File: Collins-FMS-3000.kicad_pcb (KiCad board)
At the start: 2 copper layers, 145 x 160 mm, 188 parts, among them J1 USB_B_Mini, J2 AVR-ISP-6, J3 Conn_01x04, SW1 SW_Push_LED, SW10 SW_Push_LED, SW11 SW_Push_LED, SW12 SW_Push_LED, SW13 SW_Push_LED, SW14 SW_Push_LED, SW15 SW_Push_LED, SW16 SW_Push_LED, SW17 SW_Push_LED, SW18 SW_Push_LED, SW19 SW_Push_LED, SW2 SW_Push_LED, SW20 SW_Push_LED, SW21 SW_Push_LED, SW22 SW_Push_LED, SW23 SW_Push_LED, SW24 SW_Push_LED, SW25 SW_Push_LED, SW26 SW_Push_LED, SW27 SW_Push_LED, SW28 SW_Push_LED, SW29 SW_Push_LED, SW3 SW_Push_LED, SW30 SW_Push_LED, SW31 SW_Push_LED, SW32 SW_Push_LED, SW33 SW_Push_LED, SW34 SW_Push_LED, SW35 SW_Push_LED, SW36 SW_Push_LED, SW37 SW_Push_LED, SW38 SW_Push_LED, SW39 SW_Push_LED, SW4 SW_Push_LED, SW40 SW_Push_LED, SW41 SW_Push_LED, SW42 SW_Push_LED, SW43 SW_Push_LED, SW44 SW_Push_LED, SW45 SW_Push_LED, SW46 SW_Push_LED, SW47 SW_Push_LED, SW48 SW_Push_LED, SW49 SW_Push_LED, SW5 SW_Push_LED, SW50 SW_Push_LED, SW51 SW_Push_LED, SW52 SW_Push_LED, SW53 SW_Push_LED, SW54 SW_Push_LED, SW55 SW_Push_LED, SW56 SW_Push_LED, SW57 SW_Push_LED, SW58 SW_Push_LED, SW59 SW_Push_LED, SW6 SW_Push_LED, SW60 SW_Push_LED, SW61 SW_Push_LED, SW62 SW_Push_LED, SW63 SW_Push_LED, SW64 SW_Push_LED, SW65 SW_Push_LED, SW66 SW_Push_LED, SW67 SW_Push_LED, SW68 SW_Push_LED, SW69 SW_Push_LED, SW7 SW_Push_LED, SW70 SW_Push, SW8 SW_Push_LED, SW9 SW_Push_LED, U1 ATmega32U4-MU, U2 MCP23017_SO, U3 MCP23017_SO, U4 IS31FL3733B, Y1 16MHz

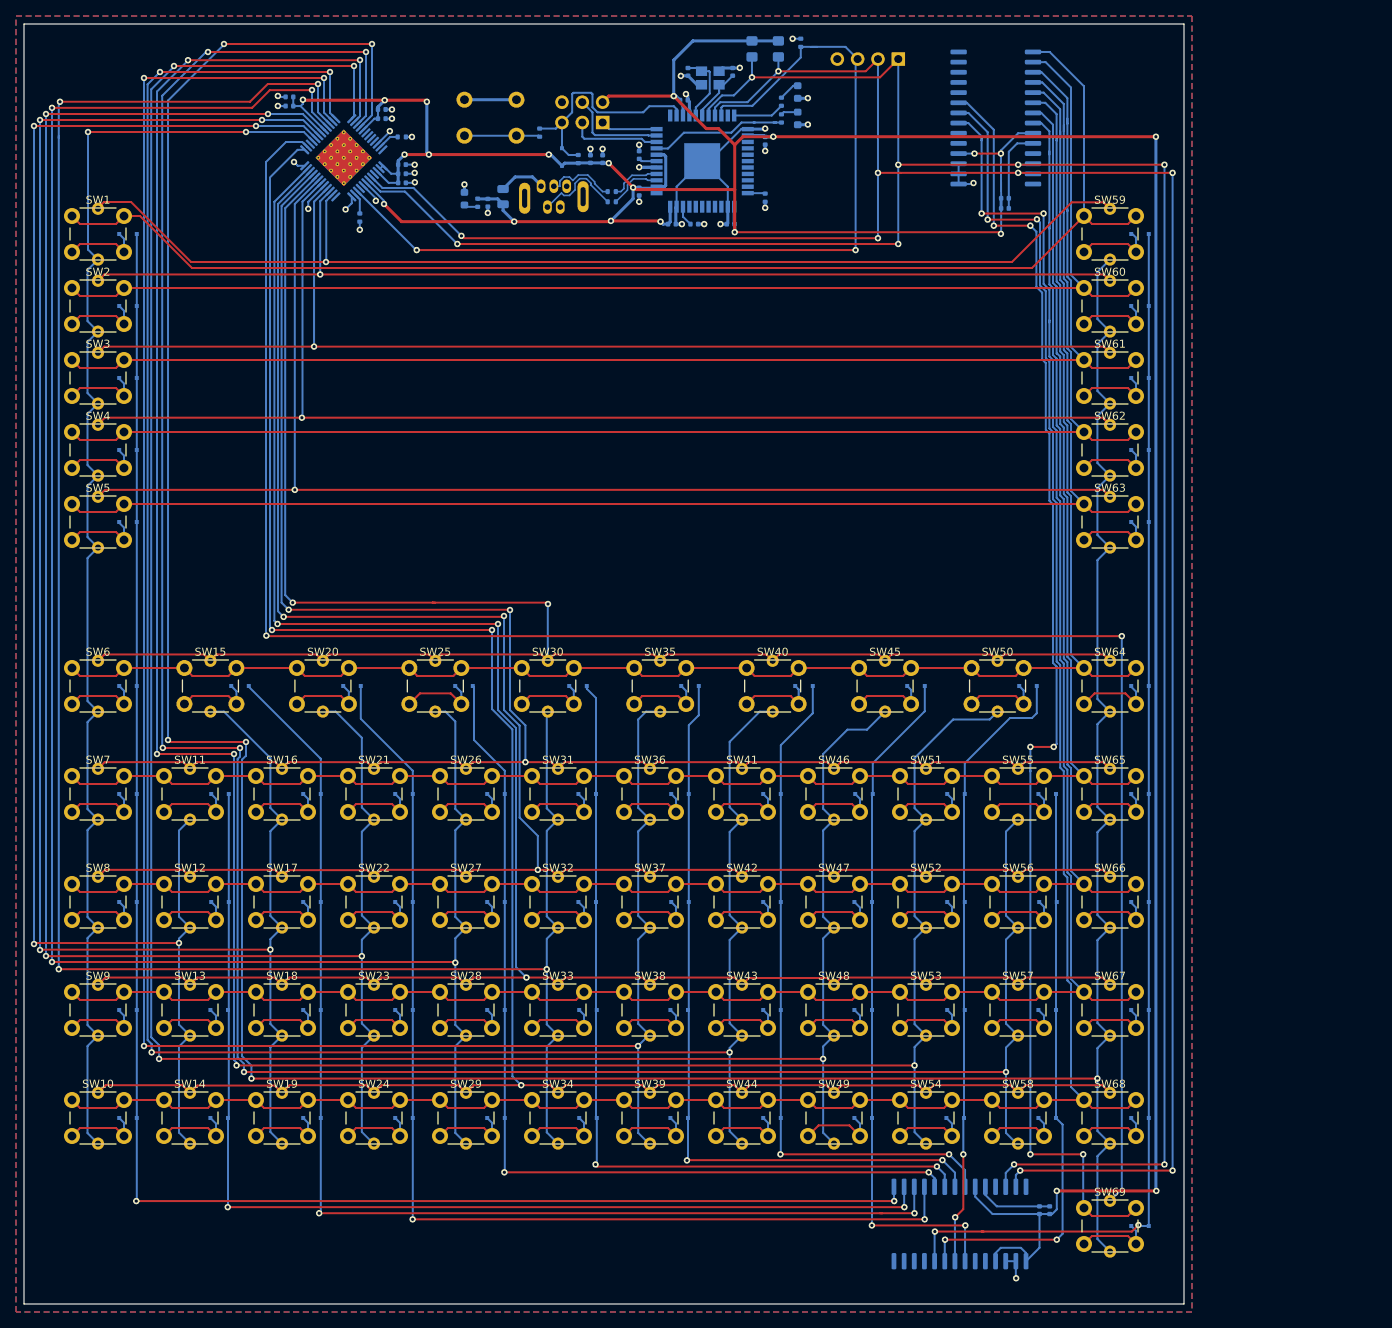
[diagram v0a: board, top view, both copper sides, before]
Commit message: Add mounting holes and silkscreen
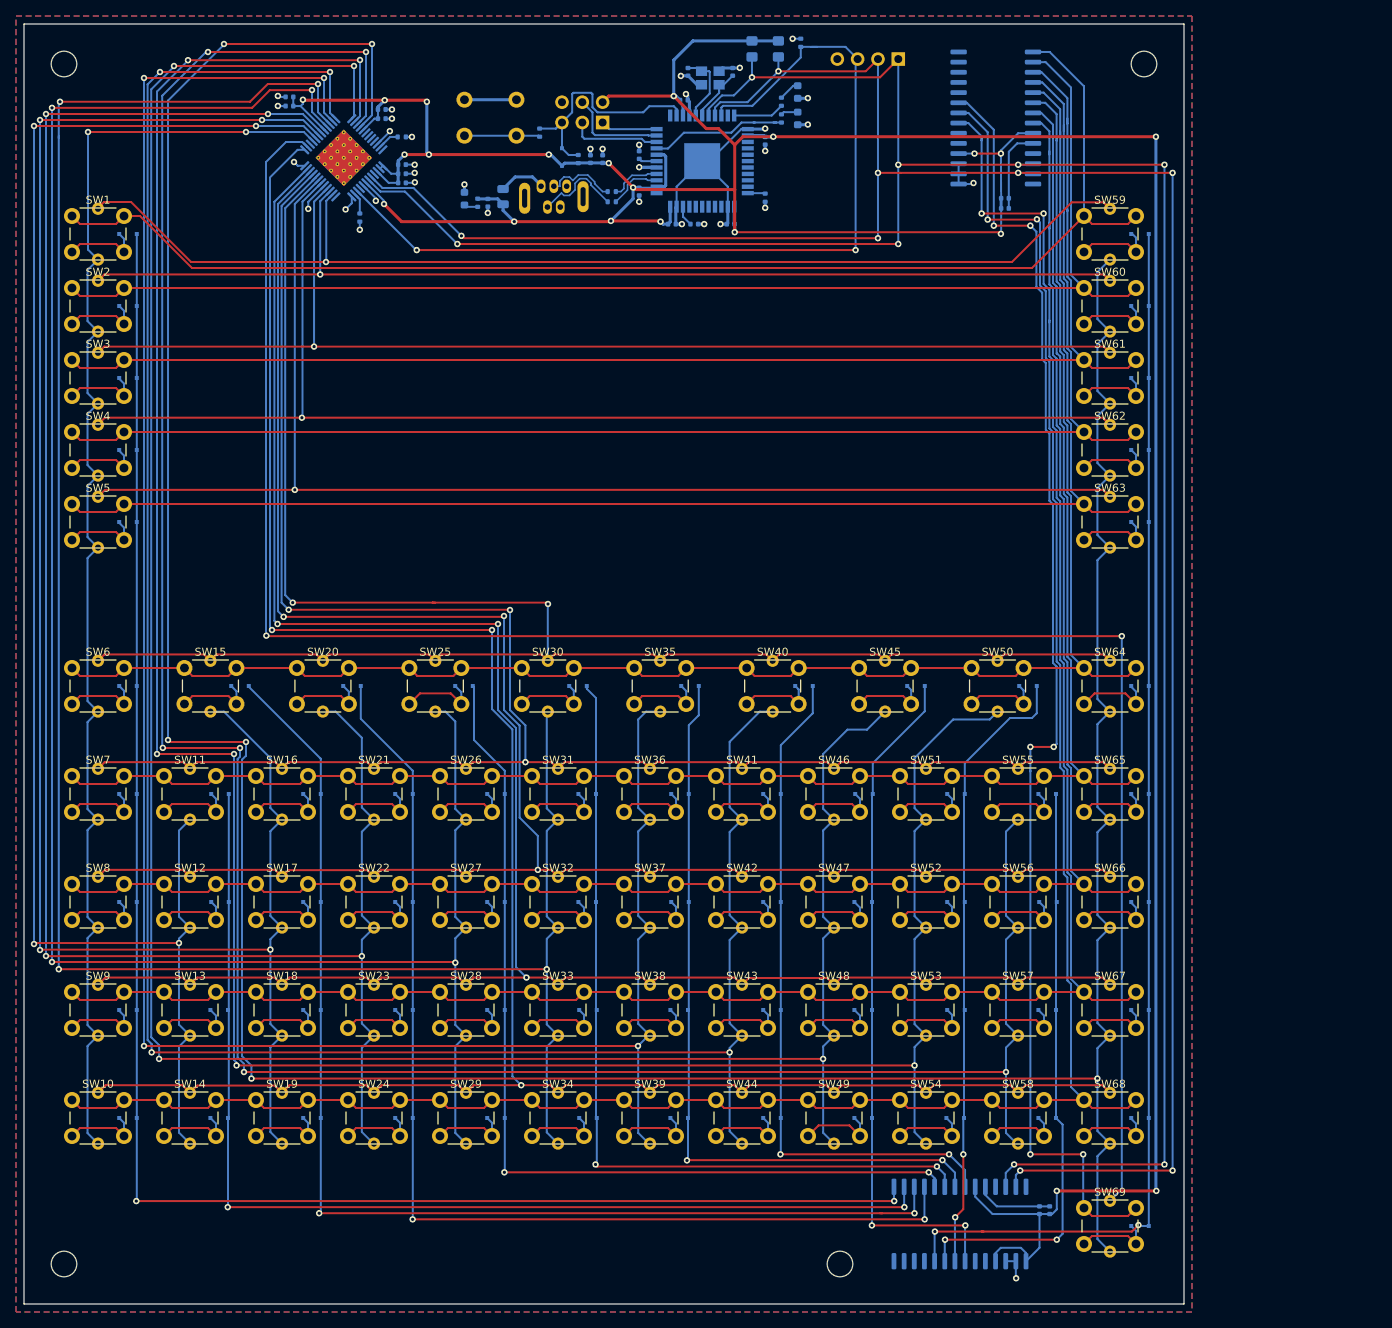
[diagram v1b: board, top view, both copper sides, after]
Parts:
- added H1: MountingHole, MountingHole:MountingHole_3.2mm_M3, F.Cu at (25.0, 25.0)
- added H2: MountingHole, MountingHole:MountingHole_3.2mm_M3, F.Cu at (160.0, 25.0)
- added H3: MountingHole, MountingHole:MountingHole_3.2mm_M3, F.Cu at (25.0, 175.0)
- added H4: MountingHole, MountingHole:MountingHole_3.2mm_M3, F.Cu at (122.0, 175.0)
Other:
- board text added: "+5V"
- board text added: "GND"
- board text added: "MISO"
- board text added: "MOSI"
- board text added: "RESET"
- board text added: "SCK"
- board text added: "SCL"
- board text added: "SDA"
- board text added: "SDB"

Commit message: Fix the button layout. Still needs trace work.
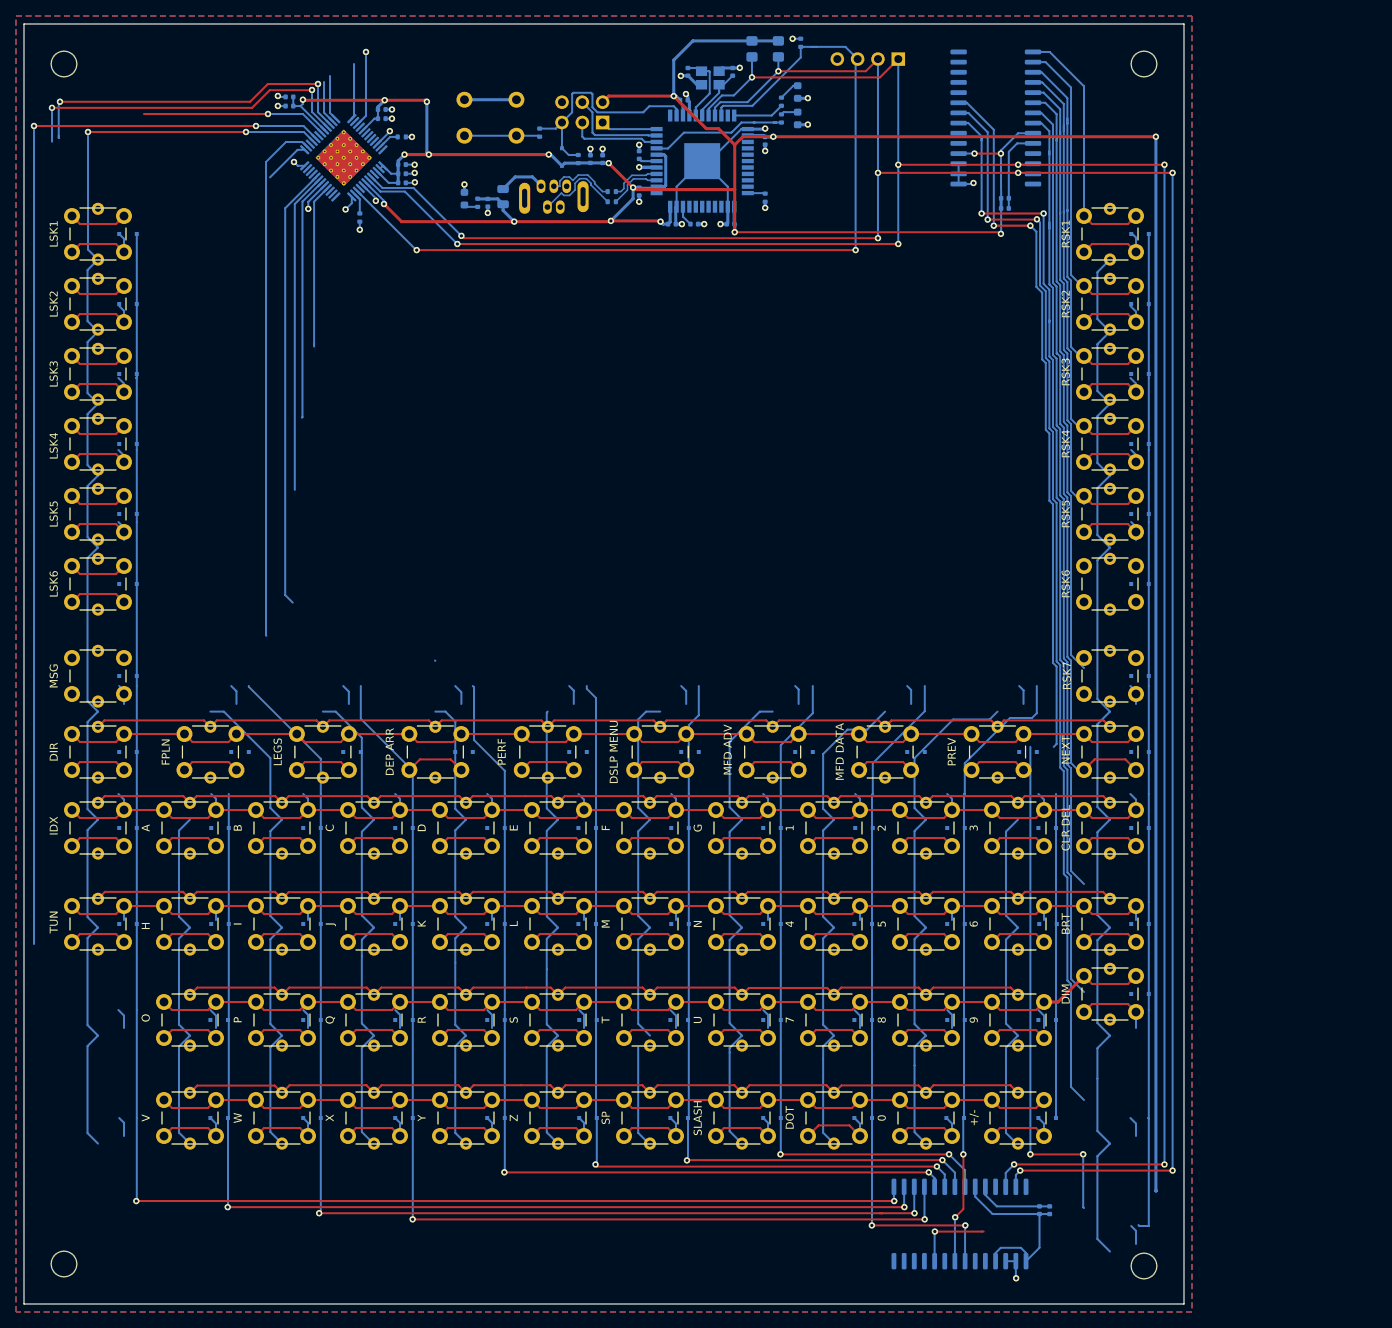
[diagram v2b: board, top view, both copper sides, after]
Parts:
- removed the D10 at (33.0, 156.8)
- removed the D68 at (159.5, 156.8)
- removed the D69 at (159.5, 170.2)
- removed the D9 at (33.0, 143.2)
- removed SW10, SW68, SW69, SW9: SW_Push_LED, Collins-FMS-3000:SW_PUSH_6mm
- added D6: D_Small, Diode_SMD:D_SOD-323F, B.Cu at (33.0, 90.0)
- added D64: D_Small, Diode_SMD:D_SOD-323F, B.Cu at (159.5, 90.0)
- added D65: D_Small, Diode_SMD:D_SOD-323F, B.Cu at (159.5, 101.5)
- added D7: D_Small, Diode_SMD:D_SOD-323F, B.Cu at (33.0, 101.5)
- added LSK6: SW_Push_LED, Collins-FMS-3000:SW_PUSH_6mm, F.Cu at (26.0, 87.8)
- added MSG: SW_Push_LED, Collins-FMS-3000:SW_PUSH_6mm, F.Cu at (26.0, 99.2)
- added RSK6: SW_Push_LED, Collins-FMS-3000:SW_PUSH_6mm, F.Cu at (152.5, 87.8)
- added RSK7: SW_Push_LED, Collins-FMS-3000:SW_PUSH_6mm, F.Cu at (152.5, 99.2)
- CLR DEL: renamed from SW65
- DEP ARR: renamed from SW25
- DSLP MENU: renamed from SW35
- MFD ADV: renamed from SW40
- MFD DATA: renamed from SW45
- moved H4 38.0 mm to (160.0, 175.2)
- moved D15 8.25 mm to (47.0, 111.0)
- moved D20 8.25 mm to (61.0, 111.0)
- moved D25 8.25 mm to (75.0, 111.0)
- moved D30 8.25 mm to (89.2, 111.0)
- moved D35 8.25 mm to (103.2, 111.0)
- moved D40 8.25 mm to (117.5, 111.0)
- moved D45 8.25 mm to (131.5, 111.0)
- moved D50 8.25 mm to (145.5, 111.0)
- moved D66 8.25 mm to (159.5, 111.0)
- moved D8 8.25 mm to (33.0, 111.0)
- moved DEP ARR 8.25 mm to (68.2, 108.8)
- moved DIR 8.25 mm to (26.0, 108.8)
- moved DSLP MENU 8.25 mm to (96.3, 108.8)
- moved FPLN 8.25 mm to (40.1, 108.8)
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- renumbered SW58 to +/-, SW54 to 0, SW46 to 1, SW51 to 2, SW55 to 3, SW47 to 4, SW52 to 5, SW56 to 6, SW48 to 7, SW53 to 8, SW57 to 9, SW11 to A, SW16 to B, SW66 to BRT, SW21 to C, SW26 to D, D8 to D10, D64 to D66, D65 to D67, D66 to D68, D67 to D69, D6 to D8, D7 to D9, SW67 to DIM, SW6 to DIR, SW49 to DOT, SW31 to E, SW36 to F, SW15 to FPLN, SW41 to G, SW12 to H, SW17 to I, SW7 to IDX, SW22 to J, SW27 to K, SW32 to L, SW20 to LEGS, SW1 to LSK1, SW2 to LSK2, SW3 to LSK3, SW4 to LSK4, SW5 to LSK5, SW37 to M, SW42 to N, SW64 to NEXT, SW13 to O, SW18 to P, SW30 to PERF, SW50 to PREV, SW23 to Q, SW28 to R, SW59 to RSK1, SW60 to RSK2, SW61 to RSK3, SW62 to RSK4, SW63 to RSK5, SW33 to S, SW44 to SLASH, SW39 to SP, SW38 to T, SW8 to TUN, SW43 to U, SW14 to V, SW19 to W, SW24 to X, SW29 to Y, SW34 to Z
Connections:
- +/- pad 1: /ButtonMatrix/ROW9 -> /ButtonMatrix/ROW11
- +/- pad 3: /LEDMatrix/SW10 -> /LEDMatrix/SW12
- 0 pad 1: /ButtonMatrix/ROW9 -> /ButtonMatrix/ROW11
- 0 pad 3: /LEDMatrix/SW10 -> /LEDMatrix/SW12
- 1 pad 1: /ButtonMatrix/ROW6 -> /ButtonMatrix/ROW8
- 1 pad 3: /LEDMatrix/SW7 -> /LEDMatrix/SW9
- 2 pad 1: /ButtonMatrix/ROW6 -> /ButtonMatrix/ROW8
- 2 pad 3: /LEDMatrix/SW7 -> /LEDMatrix/SW9
- 3 pad 1: /ButtonMatrix/ROW6 -> /ButtonMatrix/ROW8
- 3 pad 3: /LEDMatrix/SW7 -> /LEDMatrix/SW9
- 4 pad 1: /ButtonMatrix/ROW7 -> /ButtonMatrix/ROW9
- 4 pad 3: /LEDMatrix/SW8 -> /LEDMatrix/SW10
- 5 pad 1: /ButtonMatrix/ROW7 -> /ButtonMatrix/ROW9
- 5 pad 3: /LEDMatrix/SW8 -> /LEDMatrix/SW10
- 6 pad 1: /ButtonMatrix/ROW7 -> /ButtonMatrix/ROW9
- 6 pad 3: /LEDMatrix/SW8 -> /LEDMatrix/SW10
- 7 pad 1: /ButtonMatrix/ROW8 -> /ButtonMatrix/ROW10
- 7 pad 3: /LEDMatrix/SW9 -> /LEDMatrix/SW11
- 8 pad 1: /ButtonMatrix/ROW8 -> /ButtonMatrix/ROW10
- 8 pad 3: /LEDMatrix/SW9 -> /LEDMatrix/SW11
- 9 pad 1: /ButtonMatrix/ROW8 -> /ButtonMatrix/ROW10
- 9 pad 3: /LEDMatrix/SW9 -> /LEDMatrix/SW11
- A pad 1: /ButtonMatrix/ROW6 -> /ButtonMatrix/ROW8
- A pad 3: /LEDMatrix/SW7 -> /LEDMatrix/SW9
- B pad 1: /ButtonMatrix/ROW6 -> /ButtonMatrix/ROW8
- B pad 3: /LEDMatrix/SW7 -> /LEDMatrix/SW9
- BRT pad 1: /ButtonMatrix/ROW7 -> /ButtonMatrix/ROW9
- BRT pad 3: /LEDMatrix/SW8 -> /LEDMatrix/SW10
- C pad 1: /ButtonMatrix/ROW6 -> /ButtonMatrix/ROW8
- C pad 3: /LEDMatrix/SW7 -> /LEDMatrix/SW9
- CLR DEL pad 1: /ButtonMatrix/ROW6 -> /ButtonMatrix/ROW8
- CLR DEL pad 3: /LEDMatrix/SW7 -> /LEDMatrix/SW9
- D pad 1: /ButtonMatrix/ROW6 -> /ButtonMatrix/ROW8
- D pad 3: /LEDMatrix/SW7 -> /LEDMatrix/SW9
- DEP ARR pad 1: /ButtonMatrix/ROW5 -> /ButtonMatrix/ROW7
- DEP ARR pad 3: /LEDMatrix/SW6 -> /LEDMatrix/SW8
- DIM pad 1: /ButtonMatrix/ROW8 -> /ButtonMatrix/ROW10
- DIM pad 3: /LEDMatrix/SW9 -> /LEDMatrix/SW11
- DIR pad 1: /ButtonMatrix/ROW5 -> /ButtonMatrix/ROW7
- DIR pad 3: /LEDMatrix/SW6 -> /LEDMatrix/SW8
- DOT pad 1: /ButtonMatrix/ROW9 -> /ButtonMatrix/ROW11
- DOT pad 3: /LEDMatrix/SW10 -> /LEDMatrix/SW12
- DSLP MENU pad 1: /ButtonMatrix/ROW5 -> /ButtonMatrix/ROW7
- DSLP MENU pad 3: /LEDMatrix/SW6 -> /LEDMatrix/SW8
- E pad 1: /ButtonMatrix/ROW6 -> /ButtonMatrix/ROW8
- E pad 3: /LEDMatrix/SW7 -> /LEDMatrix/SW9
- F pad 1: /ButtonMatrix/ROW6 -> /ButtonMatrix/ROW8
- F pad 3: /LEDMatrix/SW7 -> /LEDMatrix/SW9
- FPLN pad 1: /ButtonMatrix/ROW5 -> /ButtonMatrix/ROW7
- FPLN pad 3: /LEDMatrix/SW6 -> /LEDMatrix/SW8
- G pad 1: /ButtonMatrix/ROW6 -> /ButtonMatrix/ROW8
- G pad 3: /LEDMatrix/SW7 -> /LEDMatrix/SW9
- H pad 1: /ButtonMatrix/ROW7 -> /ButtonMatrix/ROW9
- H pad 3: /LEDMatrix/SW8 -> /LEDMatrix/SW10
- I pad 1: /ButtonMatrix/ROW7 -> /ButtonMatrix/ROW9
- I pad 3: /LEDMatrix/SW8 -> /LEDMatrix/SW10
- IDX pad 1: /ButtonMatrix/ROW6 -> /ButtonMatrix/ROW8
- IDX pad 3: /LEDMatrix/SW7 -> /LEDMatrix/SW9
- J pad 1: /ButtonMatrix/ROW7 -> /ButtonMatrix/ROW9
- J pad 3: /LEDMatrix/SW8 -> /LEDMatrix/SW10
- K pad 1: /ButtonMatrix/ROW7 -> /ButtonMatrix/ROW9
- K pad 3: /LEDMatrix/SW8 -> /LEDMatrix/SW10
- L pad 1: /ButtonMatrix/ROW7 -> /ButtonMatrix/ROW9
- L pad 3: /LEDMatrix/SW8 -> /LEDMatrix/SW10
- LEGS pad 1: /ButtonMatrix/ROW5 -> /ButtonMatrix/ROW7
- LEGS pad 3: /LEDMatrix/SW6 -> /LEDMatrix/SW8
- M pad 1: /ButtonMatrix/ROW7 -> /ButtonMatrix/ROW9
- M pad 3: /LEDMatrix/SW8 -> /LEDMatrix/SW10
- MFD ADV pad 1: /ButtonMatrix/ROW5 -> /ButtonMatrix/ROW7
- MFD ADV pad 3: /LEDMatrix/SW6 -> /LEDMatrix/SW8
- MFD DATA pad 1: /ButtonMatrix/ROW5 -> /ButtonMatrix/ROW7
- MFD DATA pad 3: /LEDMatrix/SW6 -> /LEDMatrix/SW8
- N pad 1: /ButtonMatrix/ROW7 -> /ButtonMatrix/ROW9
- N pad 3: /LEDMatrix/SW8 -> /LEDMatrix/SW10
- NEXT pad 1: /ButtonMatrix/ROW5 -> /ButtonMatrix/ROW7
- NEXT pad 3: /LEDMatrix/SW6 -> /LEDMatrix/SW8
- O pad 1: /ButtonMatrix/ROW8 -> /ButtonMatrix/ROW10
- O pad 3: /LEDMatrix/SW9 -> /LEDMatrix/SW11
- P pad 1: /ButtonMatrix/ROW8 -> /ButtonMatrix/ROW10
- P pad 3: /LEDMatrix/SW9 -> /LEDMatrix/SW11
- PERF pad 1: /ButtonMatrix/ROW5 -> /ButtonMatrix/ROW7
- PERF pad 3: /LEDMatrix/SW6 -> /LEDMatrix/SW8
- PREV pad 1: /ButtonMatrix/ROW5 -> /ButtonMatrix/ROW7
- PREV pad 3: /LEDMatrix/SW6 -> /LEDMatrix/SW8
- Q pad 1: /ButtonMatrix/ROW8 -> /ButtonMatrix/ROW10
- Q pad 3: /LEDMatrix/SW9 -> /LEDMatrix/SW11
- R pad 1: /ButtonMatrix/ROW8 -> /ButtonMatrix/ROW10
- R pad 3: /LEDMatrix/SW9 -> /LEDMatrix/SW11
- S pad 1: /ButtonMatrix/ROW8 -> /ButtonMatrix/ROW10
- S pad 3: /LEDMatrix/SW9 -> /LEDMatrix/SW11
- SLASH pad 1: /ButtonMatrix/ROW9 -> /ButtonMatrix/ROW11
- SLASH pad 3: /LEDMatrix/SW10 -> /LEDMatrix/SW12
- SP pad 1: /ButtonMatrix/ROW9 -> /ButtonMatrix/ROW11
- SP pad 3: /LEDMatrix/SW10 -> /LEDMatrix/SW12
- T pad 1: /ButtonMatrix/ROW8 -> /ButtonMatrix/ROW10
- T pad 3: /LEDMatrix/SW9 -> /LEDMatrix/SW11
- TUN pad 1: /ButtonMatrix/ROW7 -> /ButtonMatrix/ROW9
- TUN pad 3: /LEDMatrix/SW8 -> /LEDMatrix/SW10
- U pad 1: /ButtonMatrix/ROW8 -> /ButtonMatrix/ROW10
- U pad 3: /LEDMatrix/SW9 -> /LEDMatrix/SW11
- U2 pad 24: Net-(U2-Pad24) -> /ButtonMatrix/ROW11
- U4 pad 15: Net-(U4-Pad15) -> /LEDMatrix/SW12
- V pad 1: /ButtonMatrix/ROW9 -> /ButtonMatrix/ROW11
- V pad 3: /LEDMatrix/SW10 -> /LEDMatrix/SW12
- W pad 1: /ButtonMatrix/ROW9 -> /ButtonMatrix/ROW11
- W pad 3: /LEDMatrix/SW10 -> /LEDMatrix/SW12
- X pad 1: /ButtonMatrix/ROW9 -> /ButtonMatrix/ROW11
- X pad 3: /LEDMatrix/SW10 -> /LEDMatrix/SW12
- Y pad 1: /ButtonMatrix/ROW9 -> /ButtonMatrix/ROW11
- Y pad 3: /LEDMatrix/SW10 -> /LEDMatrix/SW12
- Z pad 1: /ButtonMatrix/ROW9 -> /ButtonMatrix/ROW11
- Z pad 3: /LEDMatrix/SW10 -> /LEDMatrix/SW12
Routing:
- net /LEDMatrix/CS12: track 414.8 -> 137.0 mm, vias 6 -> 0
- net /LEDMatrix/CS11: track 309.1 -> 54.0 mm, vias 6 -> 1
- net /LEDMatrix/CS10: track 316.4 -> 65.1 mm, vias 6 -> 0
- net /LEDMatrix/SW7: track 238.2 -> 0.00 mm, vias 3 -> 0
- net /LEDMatrix/CS9: track 300.7 -> 69.5 mm, vias 4 -> 0
- net /LEDMatrix/CS8: track 285.2 -> 67.3 mm, vias 4 -> 0
- net /LEDMatrix/CS7: track 272.2 -> 64.2 mm, vias 4 -> 0
- net /LEDMatrix/SW6: track 227.0 -> 55.2 mm, vias 2 -> 0
- net /LEDMatrix/CS3: track 230.5 -> 62.3 mm, vias 4 -> 0
- net /LEDMatrix/CS6: track 266.7 -> 101.8 mm, vias 4 -> 2
- net /LEDMatrix/CS4: track 242.2 -> 84.7 mm, vias 4 -> 1
- net /LEDMatrix/CS5: track 256.2 -> 103.2 mm, vias 4 -> 2
- net /LEDMatrix/SW10: track 283.6 -> 140.2 mm, vias 3 -> 0
- net /ButtonMatrix/ROW6: track 230.3 -> 87.4 mm
- net /LEDMatrix/SW1: track 142.3 -> 0.00 mm, vias 1 -> 0
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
